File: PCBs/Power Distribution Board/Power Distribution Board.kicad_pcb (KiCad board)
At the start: 2 copper layers, 60 x 85 mm, 114 parts, among them J1 Conn_01x01, J10 Conn_01x01, J11 Conn_01x01, J12 Conn_01x01, J13 Conn_01x01, J14 Conn_01x01, J15 Conn_01x01, J16 Conn_01x01, J17 Conn_01x01, J18 Conn_01x01, J19 Conn_01x01, J2 Conn_01x01, J20 Conn_01x01, J21 Conn_01x01, J22 Conn_01x01, J23 Conn_01x01, J24 Conn_01x01, J25 Conn_01x01, J26 Conn_01x01, J27 Conn_01x01, J28 USB_B_Mini, J29 Conn_02x05_Odd_Even, J3 Conn_01x01, J4 Conn_01x01, J5 Conn_01x01, J6 Conn_01x01, J7 Conn_01x01, J8 Conn_01x01, J9 Conn_01x01, SW1 SW_Push, U1 ACS711, U10 ACS711, U11 TLV733P, U12 ATSAMD21E16L-MFT, U2 ACS711, U3 ACS711, U4 ACS711, U5 ACS711, U6 ACS711, U7 ACS711, U8 ACS711, U9 ACS711, Y1 32.7680kHz

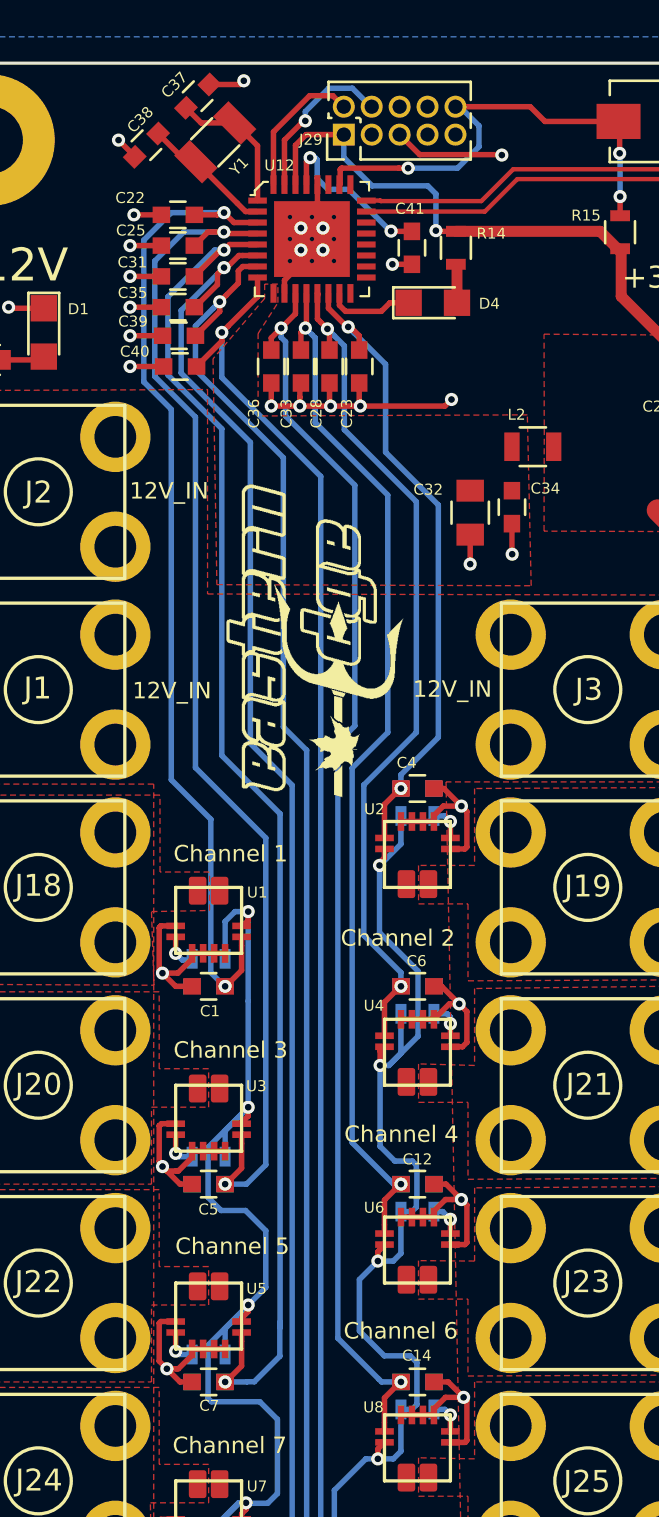
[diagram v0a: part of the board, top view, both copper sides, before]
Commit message: Minor Updates
Trying to sneak these Power PCBs through PCBWay, they caught me on a few 0.2mm drills so I made em 0.3. We'll see if my 0.2mm clearance passes their 8mil clearance (0.2035mm)
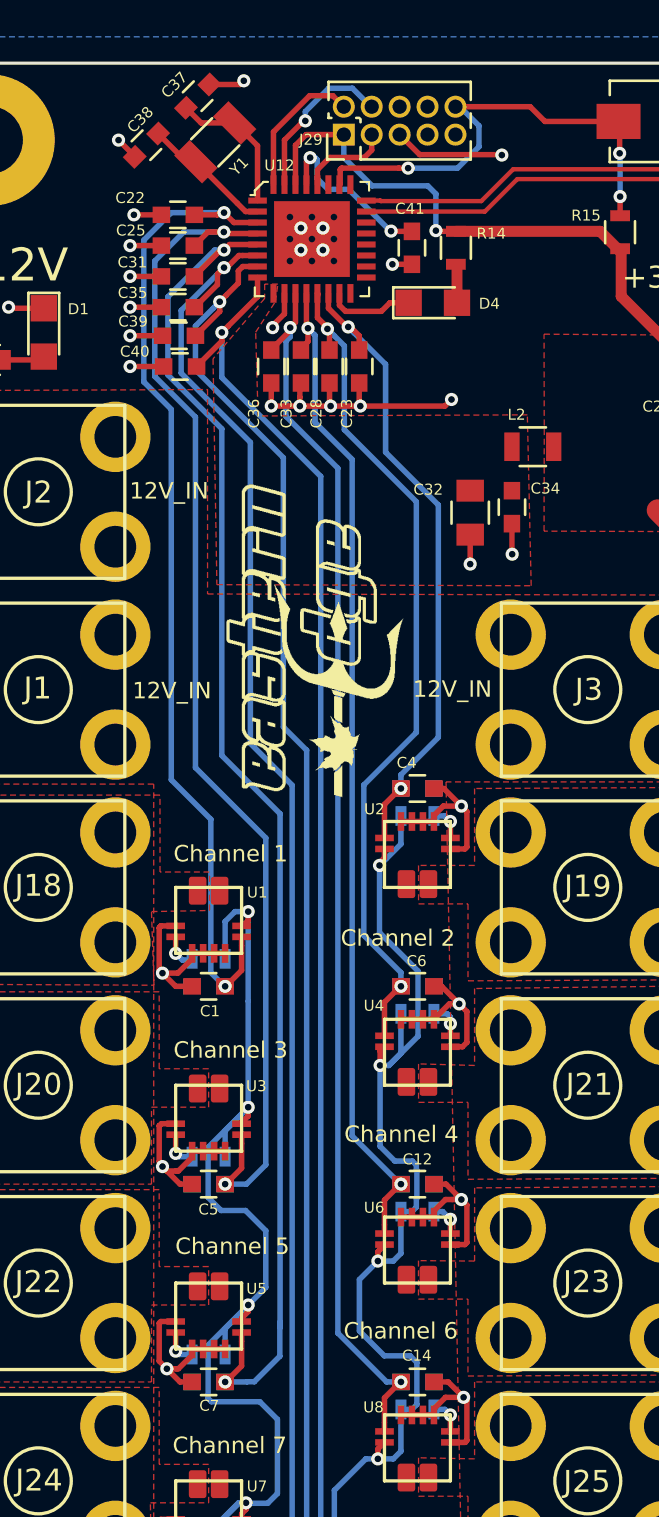
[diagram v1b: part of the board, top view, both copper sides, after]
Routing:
- net VIOUT6: track 47.5 -> 46.0 mm
- net GND: track 158.8 -> 160.0 mm, vias 40 -> 41
- net VIOUT8: track 56.9 -> 56.2 mm
